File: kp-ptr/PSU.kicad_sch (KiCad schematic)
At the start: 0 parts

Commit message: IGN & PSU added
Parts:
- added C? (x3): 1uF, symbol Device:C
- added C?: 10u, symbol Device:C
- added C?: TBD, symbol Device:C_Polarized
- added C?: 1u, symbol Device:C
- added D? (x2): G, symbol Device:LED
- added D?: D_Schottky, symbol Device:D_Schottky
- added J? (x2): Conn_01x02, symbol Connector_Generic:Conn_01x02
- added R?: 20k, symbol Device:R
- added R? (x2): 100k, symbol Device:R
- added R? (x2): 10k, symbol Device:R
- added R? (x2): DNP, symbol Device:R
- added U?: SPX3819M5-L-1-8, Package_TO_SOT_SMD:SOT-23-5, symbol Regulator_Linear:SPX3819M5-L-1-8
- added U?: SPX3819M5-L-3-3, Package_TO_SOT_SMD:SOT-23-5, symbol Regulator_Linear:SPX3819M5-L-3-3
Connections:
- new net: D?.1 (K), R?.1 (x2)
- new net: C?.1, R?.1, R?.1, R?.2
- new net +1V8: C?.1, R?.2, U?.5 (OUT)
- new net +3V3: C?.1, C?.1, D?.2 (A), R?.1, U?.1 (IN), U?.3 (EN), U?.5 (OUT)
- new net +BATT: J?.1 (Pin_1), J?.1 (Pin_1), R?.1
- new net Earth: C?.2, C?.2, C?.2, C?.2, C?.2, C?.2, J?.2 (Pin_2), R?.2, R?.2, R?.2, U?.2 (GND), U?.2 (GND)
- new net VBAT_MEAS: R?.2
- new net VCC: D?.2 (A), J?.2 (Pin_2), R?.2
- new net VDD: C?.1, C?.1, D?.1 (K), D?.2 (A), R?.1, U?.1 (IN), U?.3 (EN)
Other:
- note added: "Dajemy włącznik czy załączamy podłaczeniem akumulatora? Regulatory napięcia do dobrania. SPXy są sprawdzone w bojach, ale mogą być też inne pinowozgodne"

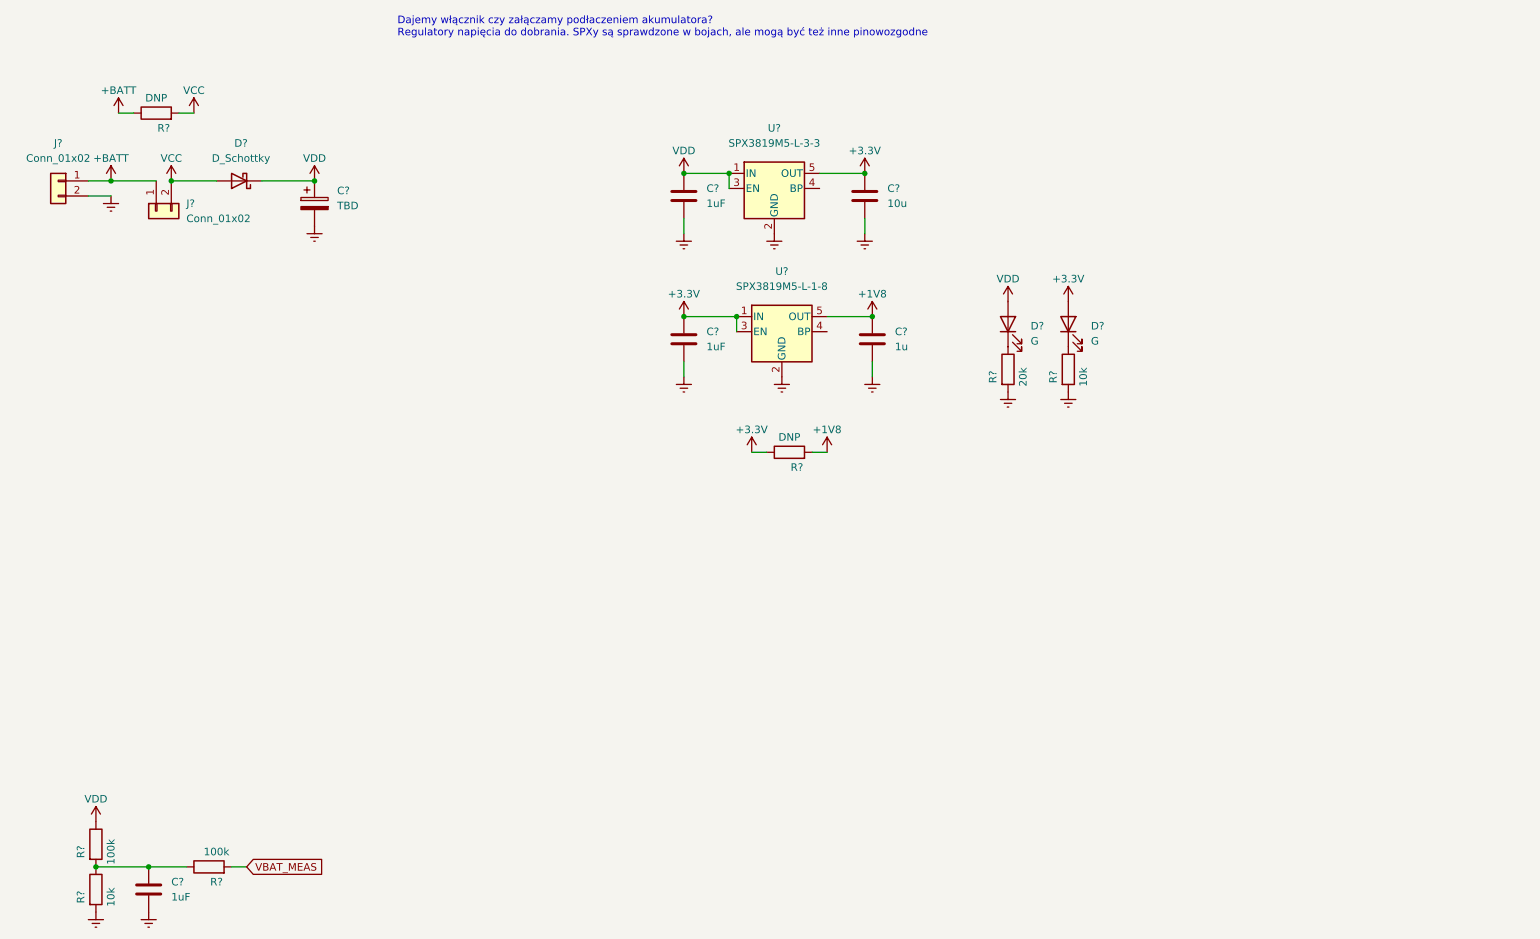
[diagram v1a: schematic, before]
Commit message: Footprints IN IMU9DOF OUT Signed-off-by: kretu <krecik@gmail.com>
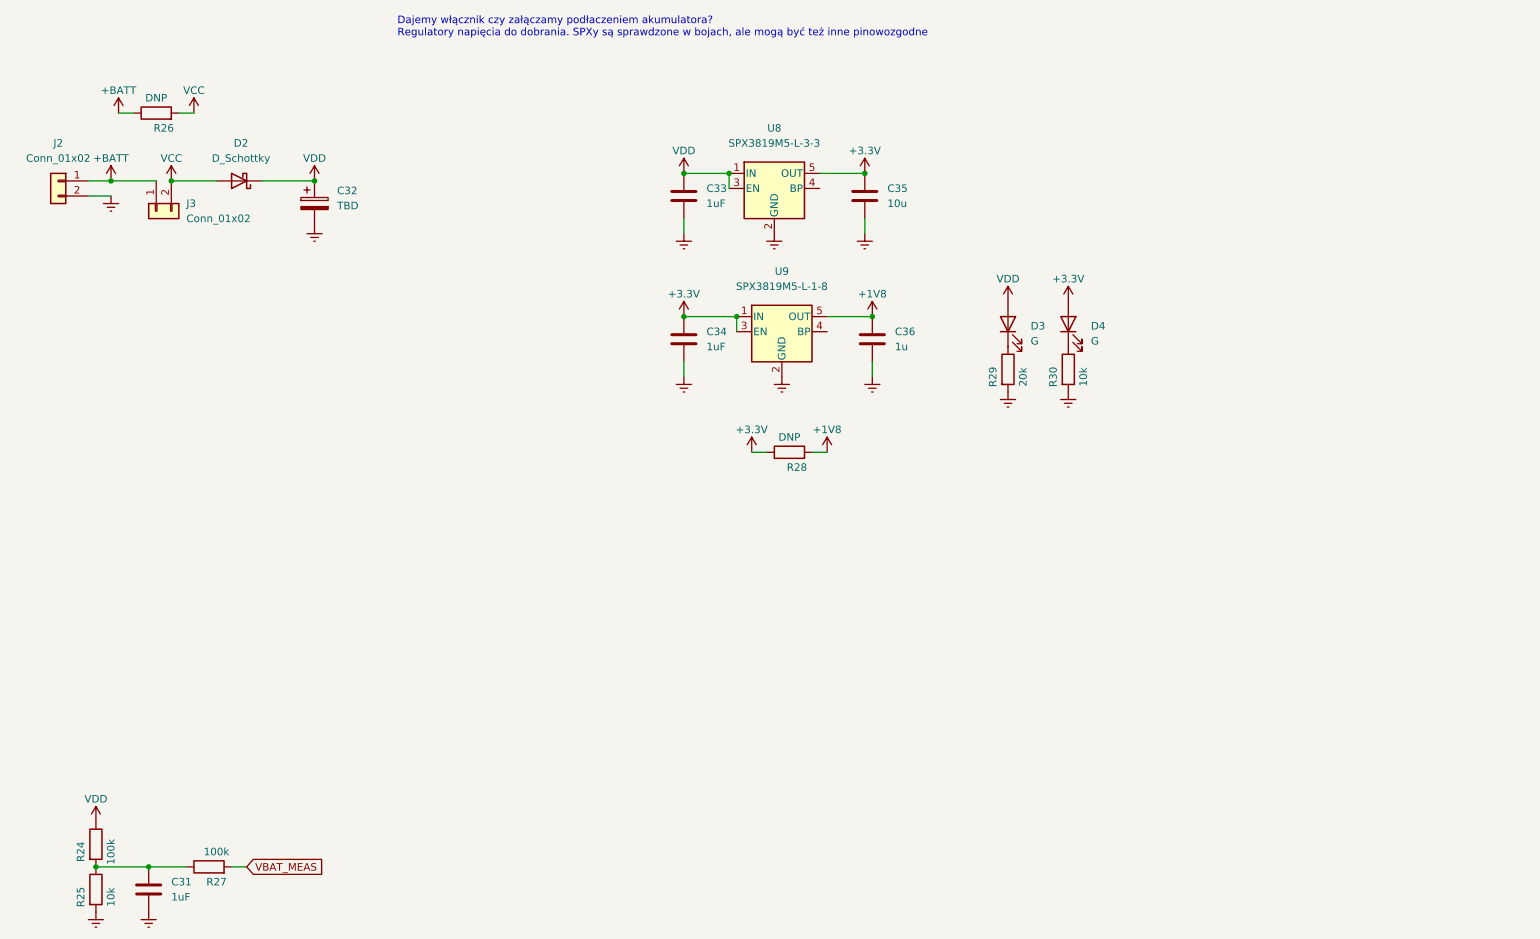
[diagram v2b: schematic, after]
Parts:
- C31, C32, C33, C34, C35, C36: renamed from C?; footprint (none) -> Capacitor_SMD:C_01005_0402Metric_Pad0.57x0.30mm_HandSolder
- J2, J3: renamed from J?; footprint (none) -> TerminalBlock_TE-Connectivity:TerminalBlock_TE_282834-2_1x02_P2.54mm_Horizontal
- R24, R25, R26, R27, R28, R29, R30: renamed from R?; footprint (none) -> Resistor_SMD:R_0402_1005Metric_Pad0.72x0.64mm_HandSolder
- gave numbers to parts that had none: 5

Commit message: Golaiath fight with board Signed-off-by: kretu <krecik@gmail.com>
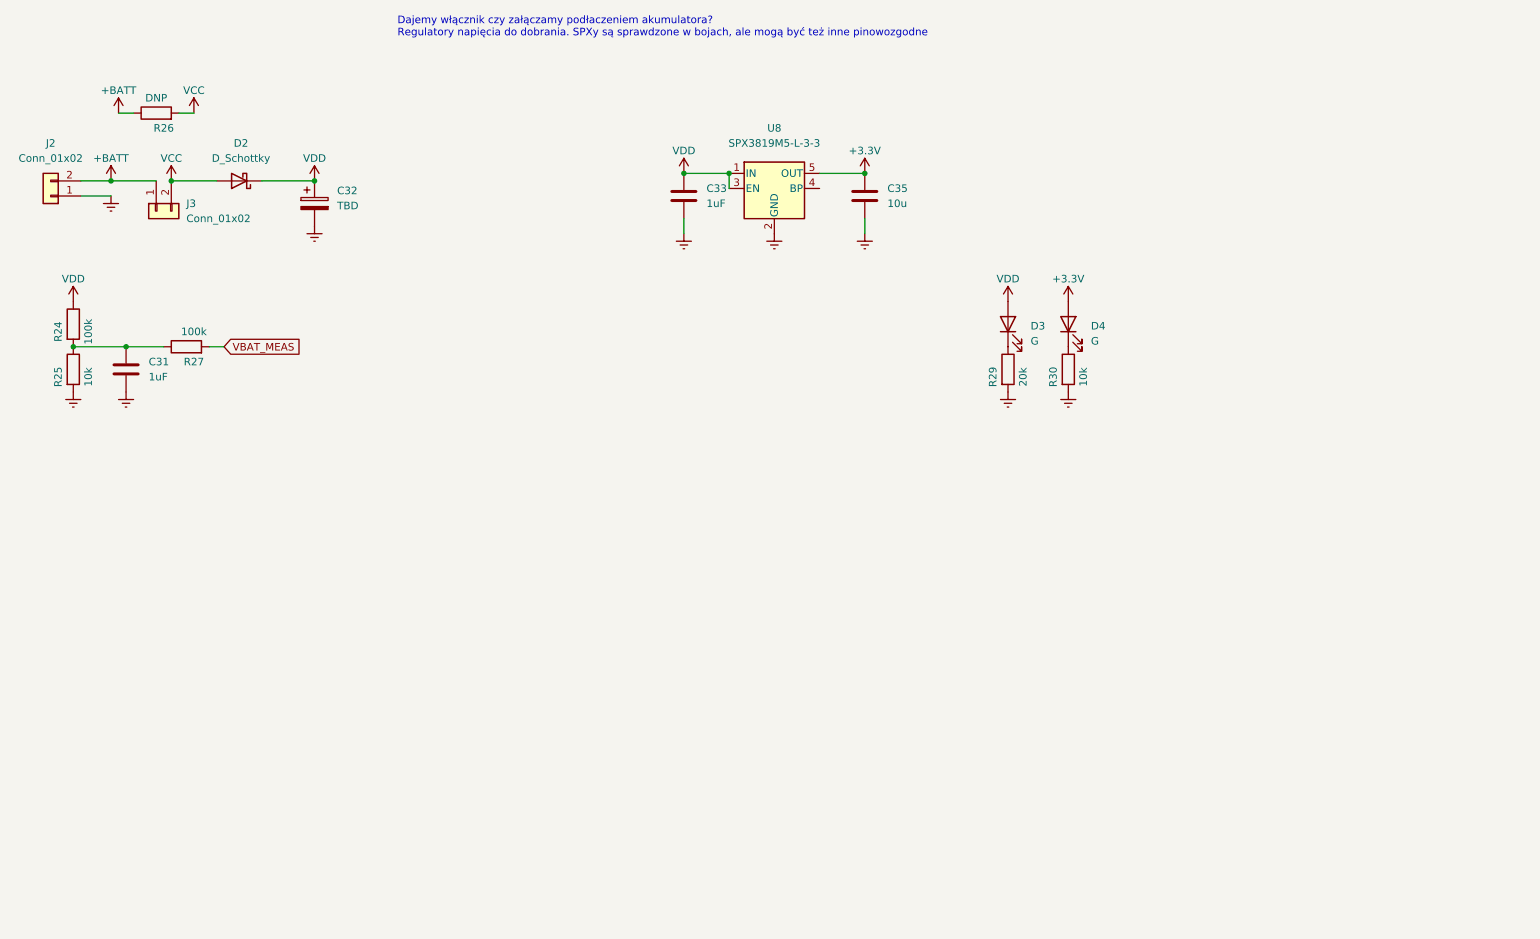
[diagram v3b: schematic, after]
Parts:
- removed C34: 1uF, Capacitor_SMD:C_01005_0402Metric_Pad0.57x0.30mm_HandSolder, symbol Device:C
- removed C36: 1u, Capacitor_SMD:C_01005_0402Metric_Pad0.57x0.30mm_HandSolder, symbol Device:C
- removed R28: DNP, Resistor_SMD:R_0402_1005Metric_Pad0.72x0.64mm_HandSolder, symbol Device:R
- removed U9: SPX3819M5-L-1-8, Package_TO_SOT_SMD:SOT-23-5, symbol Regulator_Linear:SPX3819M5-L-1-8
- D2: footprint (none) -> Diode_SMD:D_0805_2012Metric_Pad1.15x1.40mm_HandSolder
- D3, D4: footprint (none) -> LED_SMD:LED_0402_1005Metric_Pad0.77x0.64mm_HandSolder
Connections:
- net +BATT: now also J2.2 (Pin_2); no longer J2.1 (Pin_1)
- net Earth: now also J2.1 (Pin_1); no longer J2.2 (Pin_2)
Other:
- moved on the sheet: C31, J2, R24, R25, R27

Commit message: Footprinty drobnicy
Signed-off-by: kretu <krecik@gmail.com>
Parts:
- C31, C32, C33, C35: footprint Capacitor_SMD:C_01005_0402Metric_Pad0.57x0.30mm_HandSolder -> Capacitor_SMD:C_0402_1005Metric_Pad0.74x0.62mm_HandSolder
- D2: footprint Diode_SMD:D_0805_2012Metric_Pad1.15x1.40mm_HandSolder -> Diode_SMD:D_SOD-123
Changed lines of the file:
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@@
       (effects (font (size 1.27 1.27)) (justify left))
     )
-    (property "Footprint" "Capacitor_SMD:C_01005_0402Metric_Pad0.57x0.30mm_HandSolder" (id 2) (at 159.7152 50.8 0)
+    (property "Footprint" "Capacitor_SMD:C_0402_1005Metric_Pad0.74x0.62mm_HandSolder" (id 2) (at 159.7152 50.8 0)
       (effects (font (size 1.27 1.27)) hide)
     )
@@
     (property "Reference" "D2" (id 0) (at 53.6575 38.1 0))
     (property "Value" "D_Schottky" (id 1) (at 53.6575 40.64 0))
-    (property "Footprint" "Diode_SMD:D_0805_2012Metric_Pad1.15x1.40mm_HandSolder" (id 2) (at 53.34 44.45 0)
+    (property "Footprint" "Diode_SMD:D_SOD-123" (id 2) (at 53.34 44.45 0)
       (effects (font (size 1.27 1.27)) hide)
     )
@@
       (effects (font (size 1.27 1.27)) (justify left))
     )
-    (property "Footprint" "Capacitor_SMD:C_01005_0402Metric_Pad0.57x0.30mm_HandSolder" (id 2) (at 129.2352 50.8 0)
+    (property "Footprint" "Capacitor_SMD:C_0402_1005Metric_Pad0.74x0.62mm_HandSolder" (id 2) (at 129.2352 50.8 0)
       (effects (font (size 1.27 1.27)) hide)
     )
@@
       (effects (font (size 1.27 1.27)) (justify left))
     )
-    (property "Footprint" "Capacitor_SMD:C_01005_0402Metric_Pad0.57x0.30mm_HandSolder" (id 2) (at 67.0052 52.07 0)
+    (property "Footprint" "Capacitor_SMD:C_0402_1005Metric_Pad0.74x0.62mm_HandSolder" (id 2) (at 67.0052 52.07 0)
       (effects (font (size 1.27 1.27)) hide)
     )
@@
       (effects (font (size 1.27 1.27)) (justify left))
     )
-    (property "Footprint" "Capacitor_SMD:C_01005_0402Metric_Pad0.57x0.30mm_HandSolder" (id 2) (at 35.2552 80.01 0)
-      (effects (font (size 1.27 1.27)) hide)
-    )
+    (property "Footprint" "Capacitor_SMD:C_0402_1005Metric_Pad0.74x0.62mm_HandSolder" (id 2) (at 35.2552 80.01 0)
+      (effects (font (size 1.27 1.27)) hide)
+    )

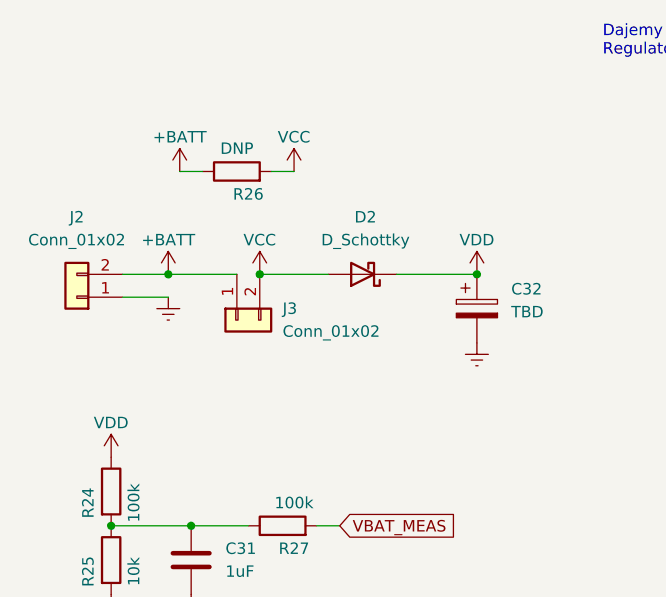
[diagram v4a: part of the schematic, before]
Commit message: Kilka zmian.
-dodany tranzystor P/N mosfet do biblioteki i zapalników
-dodany komentarz o impedancji ścieżek RF
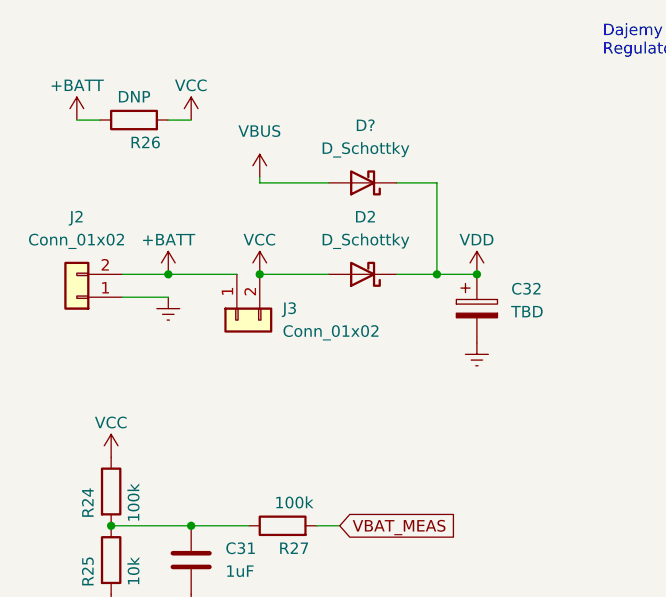
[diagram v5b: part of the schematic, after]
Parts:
- added D?: D_Schottky, Diode_SMD:D_SOD-123, symbol Device:D_Schottky
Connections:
- net VCC: now also R24.1
- net VDD: now also D?.1 (K); no longer R24.1
- new net VBUS: D?.2 (A)
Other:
- moved on the sheet: R26
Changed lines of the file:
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@@
   (junction (at 34.29 72.39) (diameter 0) (color 0 0 0 0)
   )
+  (junction (at 61.595 44.45) (diameter 0) (color 0 0 0 0)
+  )
   (junction (at 135.89 43.18) (diameter 0) (color 0 0 0 0)
   )
@@
   (junction (at 25.4 72.39) (diameter 0) (color 0 0 0 0)
   )
-  (wire (pts (xy 33.02 33.02) (xy 35.56 33.02))
+  (wire (pts (xy 21.59 27.305) (xy 24.13 27.305))
+    (stroke (width 0) (type default) (color 0 0 0 0))
+  )
+  (wire (pts (xy 57.15 34.29) (xy 61.595 34.29))
+    (stroke (width 0) (type default) (color 0 0 0 0))
+  )
+  (wire (pts (xy 41.91 34.29) (xy 41.91 33.655))
+    (stroke (width 0) (type default) (color 0 0 0 0))
+  )
+  (wire (pts (xy 61.595 44.45) (xy 66.04 44.45))
     (stroke (width 0) (type default) (color 0 0 0 0))
   )
@@
     (stroke (width 0) (type default) (color 0 0 0 0))
   )
+  (wire (pts (xy 49.53 34.29) (xy 41.91 34.29))
+    (stroke (width 0) (type default) (color 0 0 0 0))
+  )
   (wire (pts (xy 128.27 43.18) (xy 135.89 43.18))
     (stroke (width 0) (type default) (color 0 0 0 0))
   )
+  (wire (pts (xy 61.595 34.29) (xy 61.595 44.45))
+    (stroke (width 0) (type default) (color 0 0 0 0))
+  )
   (wire (pts (xy 41.91 44.45) (xy 49.53 44.45))
     (stroke (width 0) (type default) (color 0 0 0 0))
   )
-  (wire (pts (xy 57.15 44.45) (xy 66.04 44.45))
+  (wire (pts (xy 57.15 44.45) (xy 61.595 44.45))
     (stroke (width 0) (type default) (color 0 0 0 0))
   )
@@
     (stroke (width 0) (type default) (color 0 0 0 0))
   )
-  (wire (pts (xy 43.18 33.02) (xy 45.72 33.02))
+  (wire (pts (xy 31.75 27.305) (xy 34.29 27.305))
     (stroke (width 0) (type default) (color 0 0 0 0))
   )
@@
     (pin "2")
   )
+  (symbol (lib_id "power:VBUS") (at 41.91 33.655 0) (unit 1)
+    (in_bom yes) (on_board yes) (fields_autoplaced)
+    (property "Reference" "#PWR?" (id 0) (at 41.91 37.465 0)
+      (effects (font (size 1.27 1.27)) hide)
+    )
+    (property "Value" "VBUS" (id 1) (at 41.91 28.575 0))
+    (property "Footprint" "" (id 2) (at 41.91 33.655 0)
+      (effects (font (size 1.27 1.27)) hide)
+    )
+    (property "Datasheet" "" (id 3) (at 41.91 33.655 0)
+      (effects (font (size 1.27 1.27)) hide)
+    )
+    (pin "1")
+  )
   (symbol (lib_id "Device:R") (at 193.04 76.2 0) (unit 1)
     (in_bom yes) (on_board yes)
@@
     (pin "2")
   )
-  (symbol (lib_id "Device:R") (at 39.37 33.02 90) (unit 1)
-    (in_bom yes) (on_board yes)
-    (property "Reference" "R26" (id 0) (at 40.64 35.56 90))
-    (property "Value" "DNP" (id 1) (at 39.37 30.48 90))
-    (property "Footprint" "Resistor_SMD:R_0402_1005Metric_Pad0.72x0.64mm_HandSolder" (id 2) (at 39.37 34.798 90)
-      (effects (font (size 1.27 1.27)) hide)
-    )
-    (property "Datasheet" "~" (id 3) (at 39.37 33.02 0)
+  (symbol (lib_id "Device:R") (at 27.94 27.305 90) (unit 1)
+    (in_bom yes) (on_board yes)
+    (property "Reference" "R26" (id 0) (at 29.21 29.845 90))
+    (property "Value" "DNP" (id 1) (at 27.94 24.765 90))
+    (property "Footprint" "Resistor_SMD:R_0402_1005Metric_Pad0.72x0.64mm_HandSolder" (id 2) (at 27.94 29.083 90)
+      (effects (font (size 1.27 1.27)) hide)
+    )
+    (property "Datasheet" "~" (id 3) (at 27.94 27.305 0)
+      (effects (font (size 1.27 1.27)) hide)
+    )
+    (pin "1")
+    (pin "2")
+  )
+  (symbol (lib_id "Device:D_Schottky") (at 53.34 34.29 180) (unit 1)
+    (in_bom yes) (on_board yes) (fields_autoplaced)
+    (property "Reference" "D?" (id 0) (at 53.6575 27.94 0))
+    (property "Value" "D_Schottky" (id 1) (at 53.6575 30.48 0))
+    (property "Footprint" "Diode_SMD:D_SOD-123" (id 2) (at 53.34 34.29 0)
+      (effects (font (size 1.27 1.27)) hide)
+    )
+    (property "Datasheet" "~" (id 3) (at 53.34 34.29 0)
       (effects (font (size 1.27 1.27)) hide)
     )
@@
     )
     (property "Datasheet" "" (id 3) (at 158.75 43.18 0)
+      (effects (font (size 1.27 1.27)) hide)
+    )
+    (pin "1")
+  )
+  (symbol (lib_id "power:VCC") (at 25.4 64.77 0) (unit 1)
+    (in_bom yes) (on_board yes)
+    (property "Reference" "#PWR?" (id 0) (at 25.4 68.58 0)
+      (effects (font (size 1.27 1.27)) hide)
+    )
+    (property "Value" "VCC" (id 1) (at 25.4 60.96 0))
+    (property "Footprint" "" (id 2) (at 25.4 64.77 0)
+      (effects (font (size 1.27 1.27)) hide)
+    )
+    (property "Datasheet" "" (id 3) (at 25.4 64.77 0)
       (effects (font (size 1.27 1.27)) hide)
     )
@@
     (pin "5")
   )
-  (symbol (lib_id "power:VCC") (at 45.72 33.02 0) (unit 1)
-    (in_bom yes) (on_board yes)
-    (property "Reference" "#PWR094" (id 0) (at 45.72 36.83 0)
-      (effects (font (size 1.27 1.27)) hide)
-    )
-    (property "Value" "VCC" (id 1) (at 45.72 29.21 0))
-    (property "Footprint" "" (id 2) (at 45.72 33.02 0)
-      (effects (font (size 1.27 1.27)) hide)
-    )
-    (property "Datasheet" "" (id 3) (at 45.72 33.02 0)
+  (symbol (lib_id "power:VCC") (at 34.29 27.305 0) (unit 1)
+    (in_bom yes) (on_board yes)
+    (property "Reference" "#PWR094" (id 0) (at 34.29 31.115 0)
+      (effects (font (size 1.27 1.27)) hide)
+    )
+    (property "Value" "VCC" (id 1) (at 34.29 23.495 0))
+    (property "Footprint" "" (id 2) (at 34.29 27.305 0)
+      (effects (font (size 1.27 1.27)) hide)
+    )
+    (property "Datasheet" "" (id 3) (at 34.29 27.305 0)
       (effects (font (size 1.27 1.27)) hide)
     )
@@
     (pin "2")
   )
-  (symbol (lib_id "power:+BATT") (at 33.02 33.02 0) (unit 1)
-    (in_bom yes) (on_board yes)
-    (property "Reference" "#PWR091" (id 0) (at 33.02 36.83 0)
-      (effects (font (size 1.27 1.27)) hide)
-    )
-    (property "Value" "+BATT" (id 1) (at 33.02 29.21 0))
-    (property "Footprint" "" (id 2) (at 33.02 33.02 0)
-      (effects (font (size 1.27 1.27)) hide)
-    )
-    (property "Datasheet" "" (id 3) (at 33.02 33.02 0)
+  (symbol (lib_id "power:+BATT") (at 21.59 27.305 0) (unit 1)
+    (in_bom yes) (on_board yes)
+    (property "Reference" "#PWR091" (id 0) (at 21.59 31.115 0)
+      (effects (font (size 1.27 1.27)) hide)
+    )
+    (property "Value" "+BATT" (id 1) (at 21.59 23.495 0))
+    (property "Footprint" "" (id 2) (at 21.59 27.305 0)
+      (effects (font (size 1.27 1.27)) hide)
+    )
+    (property "Datasheet" "" (id 3) (at 21.59 27.305 0)
       (effects (font (size 1.27 1.27)) hide)
     )
@@
     (pin "2")
   )
-  (symbol (lib_id "power:VDD") (at 25.4 64.77 0) (unit 1)
-    (in_bom yes) (on_board yes)
-    (property "Reference" "#PWR087" (id 0) (at 25.4 68.58 0)
-      (effects (font (size 1.27 1.27)) hide)
-    )
-    (property "Value" "VDD" (id 1) (at 25.4 60.96 0))
-    (property "Footprint" "" (id 2) (at 25.4 64.77 0)
-      (effects (font (size 1.27 1.27)) hide)
-    )
-    (property "Datasheet" "" (id 3) (at 25.4 64.77 0)
-      (effects (font (size 1.27 1.27)) hide)
-    )
-    (pin "1")
-  )
   (symbol (lib_id "power:VDD") (at 182.88 64.77 0) (unit 1)
